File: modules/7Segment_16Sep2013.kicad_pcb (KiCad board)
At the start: 2 copper layers, 6 parts

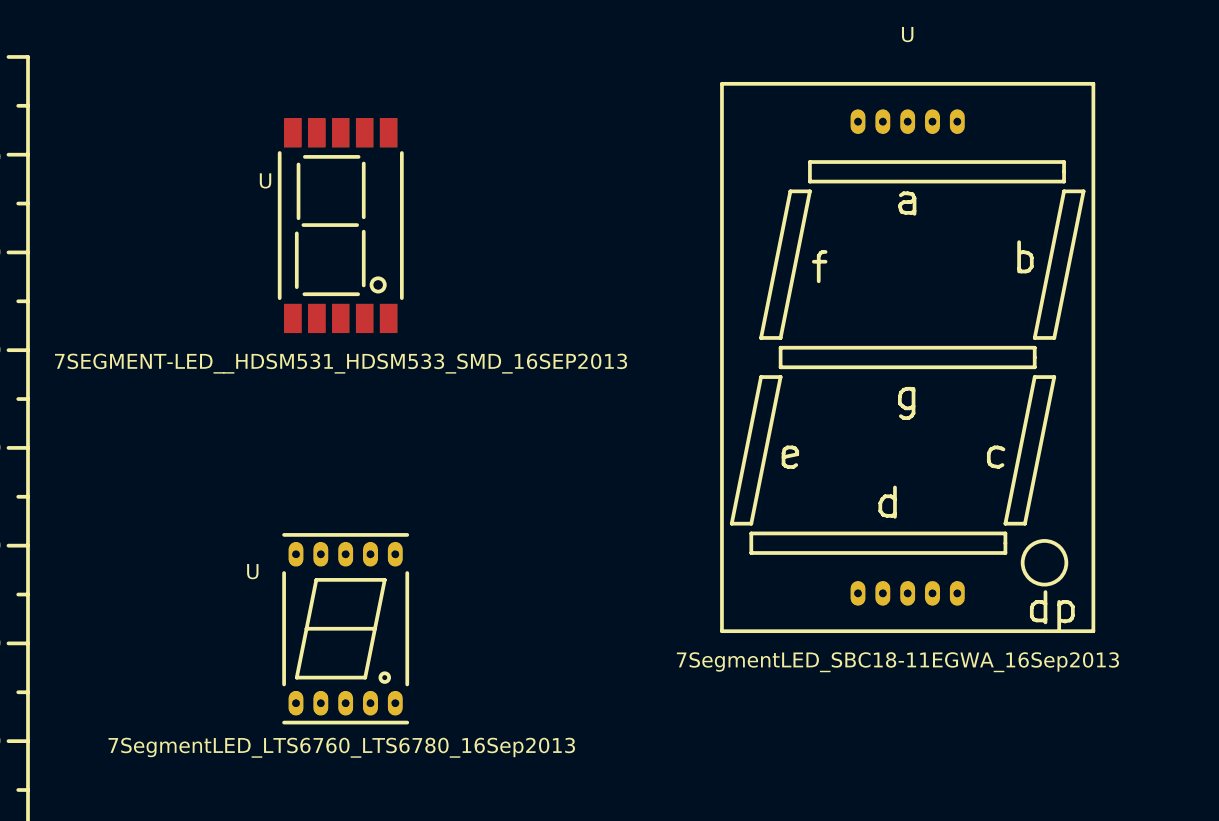
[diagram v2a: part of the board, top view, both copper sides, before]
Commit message: Some new 3D models (7-Segment and BNC-socket) and some lost(???)  .mod files
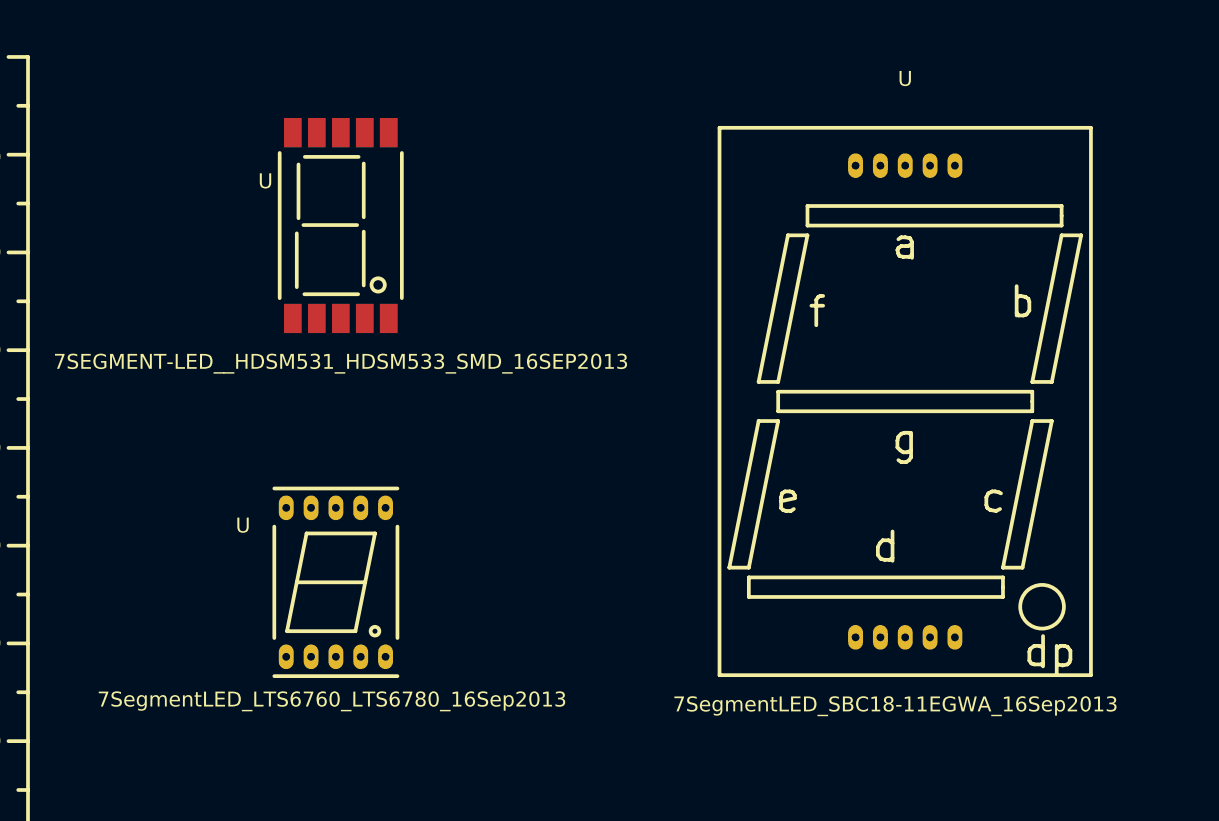
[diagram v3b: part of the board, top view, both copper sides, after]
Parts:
- moved U 4.85 mm to (117.5, 76.8)
- moved U 4.51 mm to (175.8, 58.2)

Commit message: Updates for pretty folders.
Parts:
- removed the U at (118.0, 40.2)
- added U: 7SEGMENT-LED__HDSM531_HDSM533_SMD_16SEP2013, 7-Segment:7SEGMENT-LED__HDSM531_HDSM533_SMD_16SEP2013, F.Cu at (118.5, 38.0)
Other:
- board text added: "7Segment_16Sep2013.pretty (was 7Segment_16Sep2013.mod)"
- board text added: "KiCAD Footprints of 7 segment displays from the folder"
- board text removed: "7Segment_16Sep2013.mod"
- board text removed: "KiCAD Footprints of 7 segment displays from the file"
